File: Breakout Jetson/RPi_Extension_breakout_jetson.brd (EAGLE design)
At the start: 63 x 70.1 mm, 9 parts, among them U1 CD74HC137, U2 CD74HC137

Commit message: added additional jetson breakout board just using one 1:16 multiplexer
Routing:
- net GND: track 18.2 -> 0.00 mm
- net DVCC: track 163.1 -> 160.5 mm
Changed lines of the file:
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@@
 <contactref element="SV5" pad="18"/>
 <contactref element="SV1" pad="5"/>
-<wire x1="24.83" y1="61.08" x2="24.83" y2="42.91" width="0.3048" layer="16"/>
 </signal>
 <signal name="DVCC">
@@
 <contactref element="U1" pad="16"/>
 <contactref element="U2" pad="16"/>
-<wire x1="18.85" y1="62.4" x2="47.45" y2="62.4" width="0.3048" layer="16"/>
-<via x="47.45" y="62.4" extent="1-16" drill="0.7"/>
-<wire x1="47.45" y1="62.4" x2="51.44" y2="62.4" width="0.3048" layer="1"/>
+<wire x1="18.85" y1="62.4" x2="43.55" y2="62.4" width="0.3048" layer="16"/>
+<via x="43.55" y="62.4" extent="1-16" drill="0.7"/>
+<wire x1="43.55" y1="62.4" x2="51.44" y2="62.4" width="0.3048" layer="1"/>
 <wire x1="51.44" y1="62.4" x2="52.71" y2="61.13" width="0.3048" layer="1"/>
-<wire x1="43.1194" y1="53.625" x2="45.175" y2="53.625" width="0.3048" layer="1"/>
-<wire x1="47.45" y1="55.9" x2="47.45" y2="62.4" width="0.3048" layer="1"/>
+<wire x1="43.55" y1="53.7" x2="43.55" y2="62.4" width="0.3048" layer="1"/>
 <contactref element="U1" pad="6"/>
 <contactref element="U2" pad="6"/>
@@
 <wire x1="38.675" y1="50.375" x2="41.925" y2="53.625" width="0.3048" layer="1"/>
 <wire x1="43.1194" y1="53.625" x2="41.925" y2="53.625" width="0.3048" layer="1"/>
-<wire x1="47.45" y1="55.9" x2="45.175" y2="53.625" width="0.3048" layer="1"/>
 <wire x1="18.85" y1="62.4" x2="17.55" y2="61.1" width="0.3048" layer="16"/>
 <wire x1="17.55" y1="61.1" x2="17.55" y2="54.95" width="0.3048" layer="16"/>
@@
 <wire x1="17.65" y1="53.6" x2="17.1444" y2="53.6" width="0.3048" layer="1"/>
 <wire x1="17.1444" y1="53.6" x2="17.1194" y2="53.625" width="0.3048" layer="1"/>
+<wire x1="43.1194" y1="53.625" x2="43.475" y2="53.625" width="0.3048" layer="1"/>
+<wire x1="43.475" y1="53.625" x2="43.55" y2="53.7" width="0.3048" layer="1"/>
 </signal>
 <signal name="MISO">
@@
 <contactref element="SV5" pad="36"/>
 <contactref element="U2" pad="13"/>
-<wire x1="43.1194" y1="51.674996875" x2="45.11293125" y2="51.674996875" width="0.3048" layer="1"/>
-<wire x1="45.11293125" y1="51.674996875" x2="47.65" y2="49.137928125" width="0.3048" layer="1"/>
-<wire x1="47.65" y1="42.87" x2="47.65" y2="49.137928125" width="0.3048" layer="1"/>
+<wire x1="47.65" y1="42.87" x2="47.65" y2="48.93490625" width="0.3048" layer="1"/>
+<wire x1="47.65" y1="48.93490625" x2="44.909909375" y2="51.674996875" width="0.3048" layer="1"/>
+<wire x1="44.909909375" y1="51.674996875" x2="43.1194" y2="51.674996875" width="0.3048" layer="1"/>
 </signal>
 <signal name="GPIO2">
@@
 <wire x1="45.11" y1="40.33" x2="45.13" y2="40.33" width="0.3048" layer="1"/>
 <wire x1="45.13" y1="40.33" x2="46.35" y2="41.55" width="0.3048" layer="1"/>
-<wire x1="43.1194" y1="51.025" x2="44.925" y2="51.025" width="0.3048" layer="1"/>
-<wire x1="46.35" y1="45.7" x2="46.35" y2="49.6" width="0.3048" layer="1"/>
-<wire x1="46.35" y1="49.6" x2="44.925" y2="51.025" width="0.3048" layer="1"/>
+<wire x1="46.35" y1="45.7" x2="46.35" y2="49.42324375" width="0.3048" layer="1"/>
+<wire x1="46.35" y1="49.42324375" x2="44.74824375" y2="51.025" width="0.3048" layer="1"/>
+<wire x1="44.74824375" y1="51.025" x2="43.1194" y2="51.025" width="0.3048" layer="1"/>
 <wire x1="46.35" y1="41.55" x2="46.35" y2="45.7" width="0.3048" layer="1"/>
 </signal>
@@
 <wire x1="47.65" y1="40.33" x2="47.68" y2="40.33" width="0.3048" layer="1"/>
 <wire x1="47.68" y1="40.33" x2="48.9" y2="41.55" width="0.3048" layer="1"/>
-<wire x1="43.1194" y1="52.325" x2="45.276525" y2="52.325" width="0.3048" layer="1"/>
-<wire x1="45.276525" y1="52.325" x2="48.9" y2="48.701525" width="0.3048" layer="1"/>
-<wire x1="48.9" y1="41.55" x2="48.9" y2="48.701525" width="0.3048" layer="1"/>
+<wire x1="48.9" y1="41.55" x2="48.9" y2="48.52393125" width="0.3048" layer="1"/>
+<wire x1="48.9" y1="48.52393125" x2="45.09893125" y2="52.325" width="0.3048" layer="1"/>
+<wire x1="45.09893125" y1="52.325" x2="43.1194" y2="52.325" width="0.3048" layer="1"/>
 </signal>
 <signal name="GPIO8">
@@
 <wire x1="50.19" y1="40.33" x2="50.23" y2="40.33" width="0.3048" layer="1"/>
 <wire x1="50.23" y1="40.33" x2="51.55" y2="41.65" width="0.3048" layer="1"/>
-<wire x1="43.1194" y1="52.974996875" x2="45.452496875" y2="52.974996875" width="0.3048" layer="1"/>
-<wire x1="45.452496875" y1="52.974996875" x2="51.55" y2="46.87749375" width="0.3048" layer="1"/>
-<wire x1="51.55" y1="41.65" x2="51.55" y2="46.87749375" width="0.3048" layer="1"/>
+<wire x1="51.55" y1="41.65" x2="51.55" y2="46.718353125" width="0.3048" layer="1"/>
+<wire x1="51.55" y1="46.718353125" x2="45.29335625" y2="52.974996875" width="0.3048" layer="1"/>
+<wire x1="45.29335625" y1="52.974996875" x2="43.1194" y2="52.974996875" width="0.3048" layer="1"/>
 </signal>
 <signal name="GPIO11">
@@
 <wire x1="22.29" y1="63.62" x2="22.29" y2="64.16" width="0.3048" layer="1"/>
 <wire x1="22.29" y1="64.16" x2="21.45" y2="65" width="0.3048" layer="1"/>
-<wire x1="11.4806" y1="52.975" x2="10.075" y2="52.975" width="0.3048" layer="1"/>
-<wire x1="10.075" y1="52.975" x2="9.285590625" y2="53.764409375" width="0.3048" layer="1"/>
-<wire x1="9.285590625" y1="53.764409375" x2="9.285590625" y2="58.683884375" width="0.3048" layer="1"/>
+<wire x1="11.4806" y1="52.975" x2="10.091309375" y2="52.975" width="0.3048" layer="1"/>
+<wire x1="10.091309375" y1="52.975" x2="9.285590625" y2="53.78071875" width="0.3048" layer="1"/>
+<wire x1="9.285590625" y1="53.78071875" x2="9.285590625" y2="58.683884375" width="0.3048" layer="1"/>
 <wire x1="9.285590625" y1="58.683884375" x2="15.60170625" y2="65" width="0.3048" layer="1"/>
 <wire x1="15.60170625" y1="65" x2="21.45" y2="65" width="0.3048" layer="1"/>

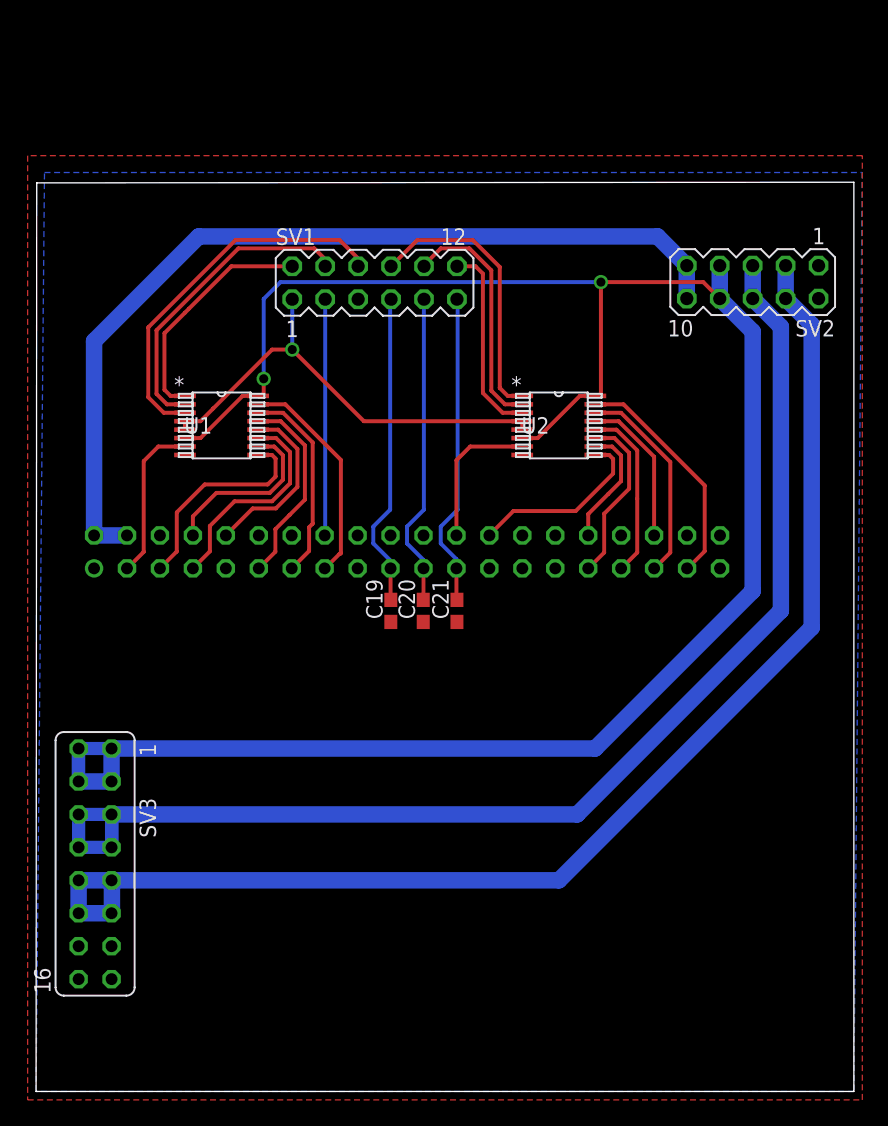
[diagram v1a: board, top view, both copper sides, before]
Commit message: changed used component to one 1 to 16 multiplexer on basic jetson tx1 board
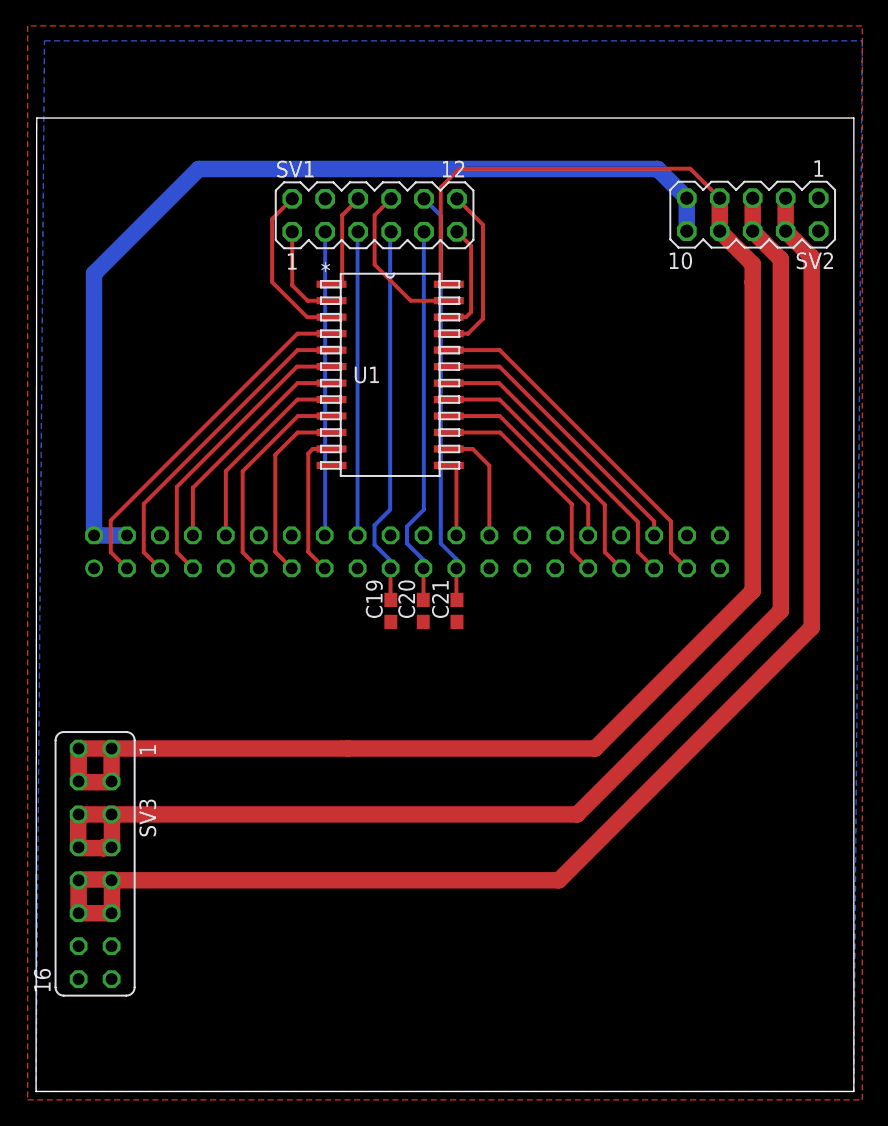
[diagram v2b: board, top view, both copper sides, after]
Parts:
- removed U2: CD74HC137, CD74HC137:PW16
- U1: value CD74HC137 -> CD74HC4515; device CD74HC137:PW16 -> CD74HC4515:DW24
- moved U1 13.6 mm to (27.3, 55.2)
- moved SV1 5.20 mm to (26.1, 67.5)
- moved SV2 5.20 mm to (55.2, 67.6)
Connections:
- removed net ADDR4: SV1.10, U2.2
- removed net ADDR5: SV1.12, U2.3
- new net ENABLE: SV1.8, U1.23
- new net LDAC: SV1.5, SV5.18
- net ADDR0: now also SV1.1, U1.2; no longer SV1.2, U1.1
- net ADDR1: now also SV1.2, U1.3; no longer SV1.4, U1.2
- net ADDR2: now also SV1.12, U1.21; no longer SV1.6, U1.3
- net ADDR3: now also SV1.11, U1.22; no longer SV1.8, U2.1
- net DVCC: now also U1.24; no longer U1.16, U1.6, U2.16, U2.6
- net GND: now also SV1.4, U1.12; no longer SV1.5, SV5.18, U1.8, U2.8
- net GPIO0: now also U1.13; no longer U2.7
- net GPIO1: now also U1.14; no longer U2.9
- net GPIO10: now also U1.17; no longer U2.12
- net GPIO11: now also U1.15; no longer U2.11
- net GPIO12: now also U1.4; no longer U1.7
- net GPIO13: now also U1.5; no longer U1.9
- net GPIO14: now also U1.8; no longer U1.12
- net GPIO15: now also U1.7; no longer U1.10
- net GPIO2: now also U1.16; no longer U2.10
- net GPIO3: now also U1.19; no longer U2.13
- net GPIO4: now also U1.6; no longer U1.11
- net GPIO5: now also U1.9; no longer U1.13
- net GPIO6: now also U1.10; no longer U1.14
- net GPIO7: now also U1.11; no longer U1.15
- net GPIO8: now also U1.20; no longer U2.15
- net GPIO9: now also U1.18; no longer U2.14
- net LATCH: now also SV1.6, U1.1; no longer SV1.1, U1.4, U1.5, U2.4, U2.5
- net SCLK: now also SV1.10; no longer SV1.11
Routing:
- net DVCC: track 160.5 -> 128.0 mm, vias 2 -> 0
- net LATCH: track 35.8 -> 7.94 mm, vias 1 -> 0
- net LDAC: track 0.00 -> 23.4 mm
- net ADDR4: track 18.6 -> 0.00 mm
- net ADDR2: track 28.9 -> 13.2 mm
- net ADDR5: track 15.1 -> 0.00 mm
- net GPIO12: track 12.5 -> 27.2 mm
- net ADDR3: track 21.4 -> 8.53 mm
- net ENABLE: track 0.00 -> 12.5 mm
- net ADDR1: track 23.9 -> 12.8 mm
- net ADDR0: track 18.1 -> 7.65 mm
- net GPIO3: track 11.7 -> 21.9 mm
- net GPIO8: track 18.0 -> 26.7 mm
- net GPIO13: track 16.5 -> 24.9 mm
- net SCLK: track 24.3 -> 32.0 mm
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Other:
- board size 63 x 70.1 mm -> 63 x 75 mm
